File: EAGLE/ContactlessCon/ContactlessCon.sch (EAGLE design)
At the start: 5 parts, among them J1 PINHEADER-212*1, J2 PINHEADER-818*1, X1 0446200002

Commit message: Conの配線終了
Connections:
- net GPIO: now also X1.5; no longer X1.3
- net SCL: now also X1.4; no longer X1.5
- net SDA: now also X1.3; no longer X1.4
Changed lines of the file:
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@@
 </segment>
 <segment>
-<pinref part="X1" gate="P" pin="3"/>
-<wire x1="98.298" y1="60.96" x2="87.122" y2="60.96" width="0.1524" layer="91"/>
-<label x="86.36" y="60.96" size="1.778" layer="95"/>
+<pinref part="X1" gate="P" pin="5"/>
+<wire x1="98.298" y1="55.88" x2="86.36" y2="55.88" width="0.1524" layer="91"/>
+<label x="86.36" y="55.88" size="1.778" layer="95"/>
 </segment>
 </net>
@@
 </segment>
 <segment>
-<pinref part="X1" gate="P" pin="5"/>
-<wire x1="98.298" y1="55.88" x2="87.122" y2="55.88" width="0.1524" layer="91"/>
-<label x="86.36" y="55.88" size="1.778" layer="95"/>
+<wire x1="98.298" y1="58.42" x2="87.122" y2="58.42" width="0.1524" layer="91"/>
+<pinref part="X1" gate="P" pin="4"/>
+<label x="86.36" y="58.42" size="1.778" layer="95"/>
 </segment>
 </net>
@@
 </segment>
 <segment>
-<wire x1="98.298" y1="58.42" x2="87.122" y2="58.42" width="0.1524" layer="91"/>
-<pinref part="X1" gate="P" pin="4"/>
-<label x="86.36" y="58.42" size="1.778" layer="95"/>
+<pinref part="X1" gate="P" pin="3"/>
+<wire x1="98.298" y1="60.96" x2="87.122" y2="60.96" width="0.1524" layer="91"/>
+<label x="86.36" y="60.96" size="1.778" layer="95"/>
 </segment>
 </net>

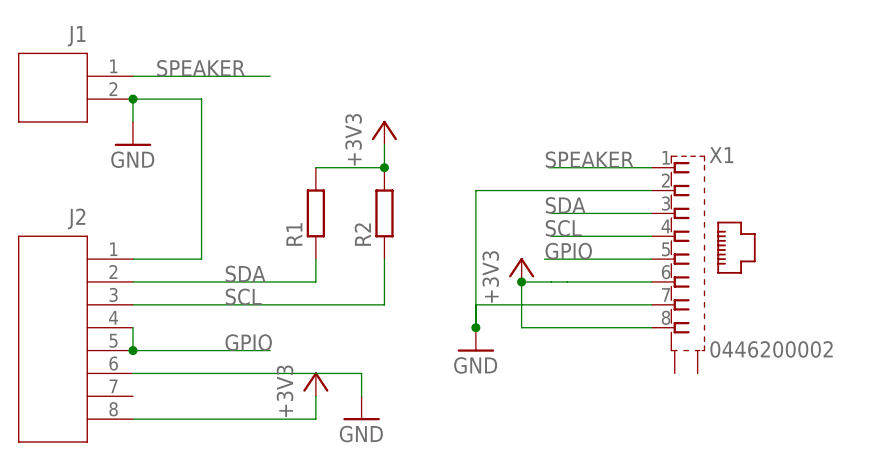
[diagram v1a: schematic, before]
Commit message: 抵抗のvalueを追加
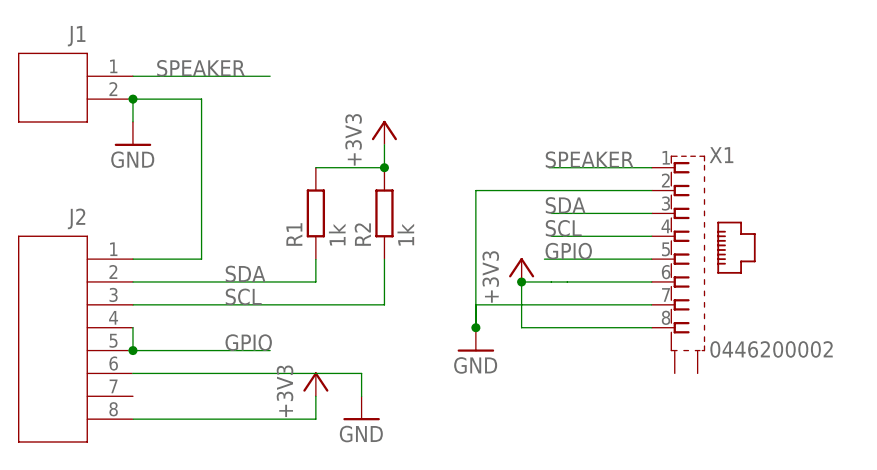
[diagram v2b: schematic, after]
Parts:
- R1, R2: value (none) -> 1k
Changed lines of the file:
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@@
 <part name="GND2" library="supply1" library_urn="urn:adsk.eagle:library:371" deviceset="GND" device=""/>
 <part name="+3V1" library="supply1" library_urn="urn:adsk.eagle:library:371" deviceset="+3V3" device=""/>
-<part name="R1" library="rcl" library_urn="urn:adsk.eagle:library:334" deviceset="R-EU_" device="R1206" package3d_urn="urn:adsk.eagle:package:23540/2"/>
-<part name="R2" library="rcl" library_urn="urn:adsk.eagle:library:334" deviceset="R-EU_" device="R1206" package3d_urn="urn:adsk.eagle:package:23540/2"/>
+<part name="R1" library="rcl" library_urn="urn:adsk.eagle:library:334" deviceset="R-EU_" device="R1206" package3d_urn="urn:adsk.eagle:package:23540/2" value="1k"/>
+<part name="R2" library="rcl" library_urn="urn:adsk.eagle:library:334" deviceset="R-EU_" device="R1206" package3d_urn="urn:adsk.eagle:package:23540/2" value="1k"/>
 <part name="+3V2" library="supply1" library_urn="urn:adsk.eagle:library:371" deviceset="+3V3" device=""/>
 <part name="+3V3" library="supply1" library_urn="urn:adsk.eagle:library:371" deviceset="+3V3" device=""/>
